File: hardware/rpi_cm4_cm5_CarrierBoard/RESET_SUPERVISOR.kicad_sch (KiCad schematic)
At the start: 34 parts, among them Q13 2N7002, Q8 2N7002, Q9 2N7002, U30 STM6710DWB6F, U31 SN74LVC1G125DBVR, U32 SN74HCS365QPWRQ1, U35 SN74HCS365QPWRQ1

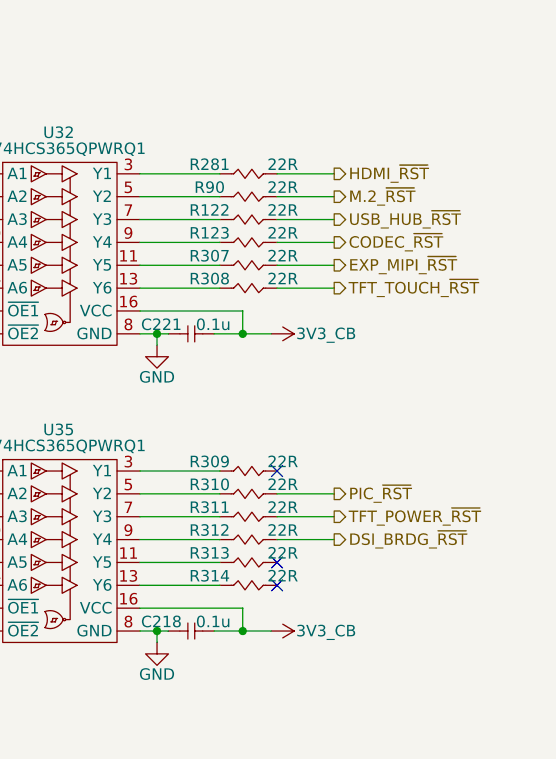
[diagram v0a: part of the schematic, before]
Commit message: Continue working on the layout. Completed most of power planes planning and pouring Completed all DiffPairs routing and length matching (preliminary)
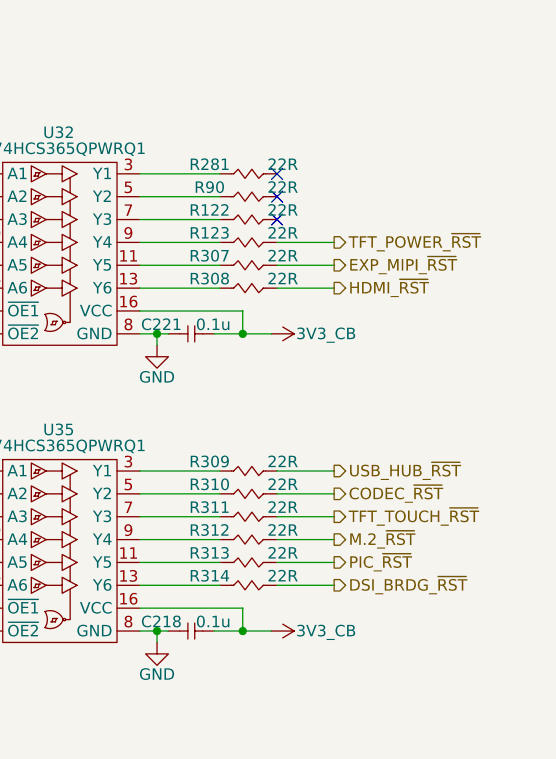
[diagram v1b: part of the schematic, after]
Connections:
- net CODEC_~{RST}: now also R310.2; no longer R123.2
- net DSI_BRDG_~{RST}: now also R314.2; no longer R312.2
- net HDMI_~{RST}: now also R308.2; no longer R281.2
- net M.2_~{RST}: now also R312.2; no longer R90.2
- net PIC_~{RST}: now also R313.2; no longer R310.2
- net TFT_POWER_~{RST}: now also R123.2; no longer R311.2
- net TFT_TOUCH_~{RST}: now also R311.2; no longer R308.2
- net USB_HUB_~{RST}: now also R309.2; no longer R122.2

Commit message: Significant update Stackup changed from 6 to 8 layers Changed design notes accordingly Re-routed all differential pairs and length match / skew match Fanout critical signals away from dense areas 95% routing completed
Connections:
- net TFT_TOUCH_~{RST}: no longer names the net of R311.2
- no-connect marks 3 -> 4
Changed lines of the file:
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@@
 	(title_block
 		(title "RPI CMx Carrier")
-		(date "2026-01-22")
+		(date "2026-02-13")
 		(rev "2.00-0A")
 		(comment 1 "Jean-Francois Bilodeau")
@@
 	)
 	(no_connect
+		(at 222.885 128.27)
+	)
+	(no_connect
 		(at 222.885 95.25)
 	)
@@
 		(pts
 			(xy 187.96 90.17) (xy 187.96 92.71)
-		)
-		(stroke
-			(width 0)
-			(type default)
-		)
-	)
-	(wire
-		(pts
-			(xy 222.885 128.27) (xy 229.235 128.27)
 		)
 		(stroke
@@
 		(effects
 			(font
-				(size 1.27 1.27)
-			)
-			(justify left)
-		)
-	)
-	(hierarchical_label "TFT_TOUCH_~{RST}"
-		(shape output)
-		(at 229.235 128.27 0)
-		(effects
-			(font

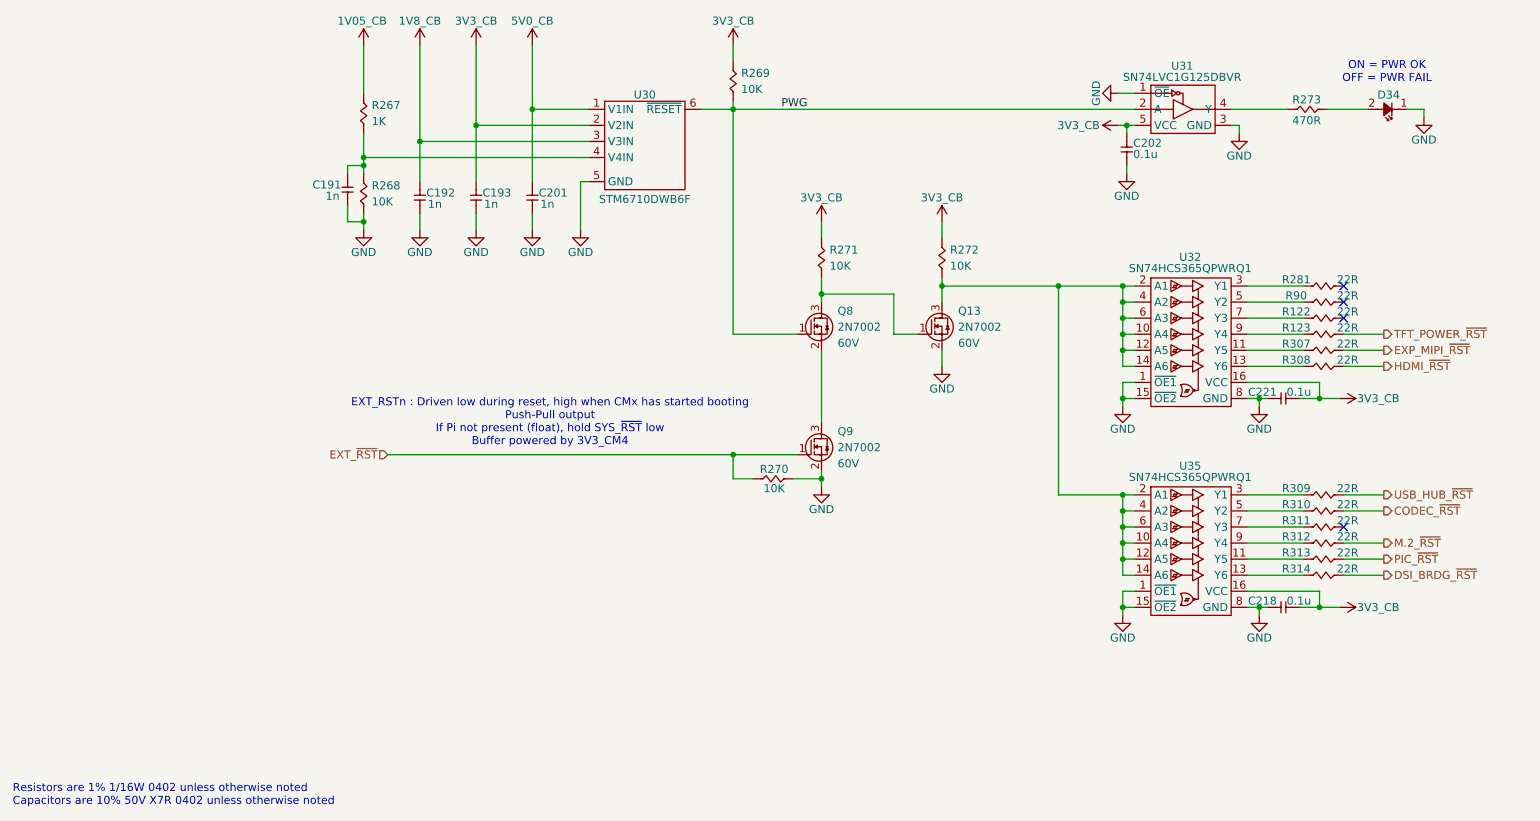
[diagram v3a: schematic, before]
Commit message: Add test points on relevant signals Re-generate SCH_PDF Re-generate BOM Re-generate all gerbers and relevant PCB output files (still in review phase)
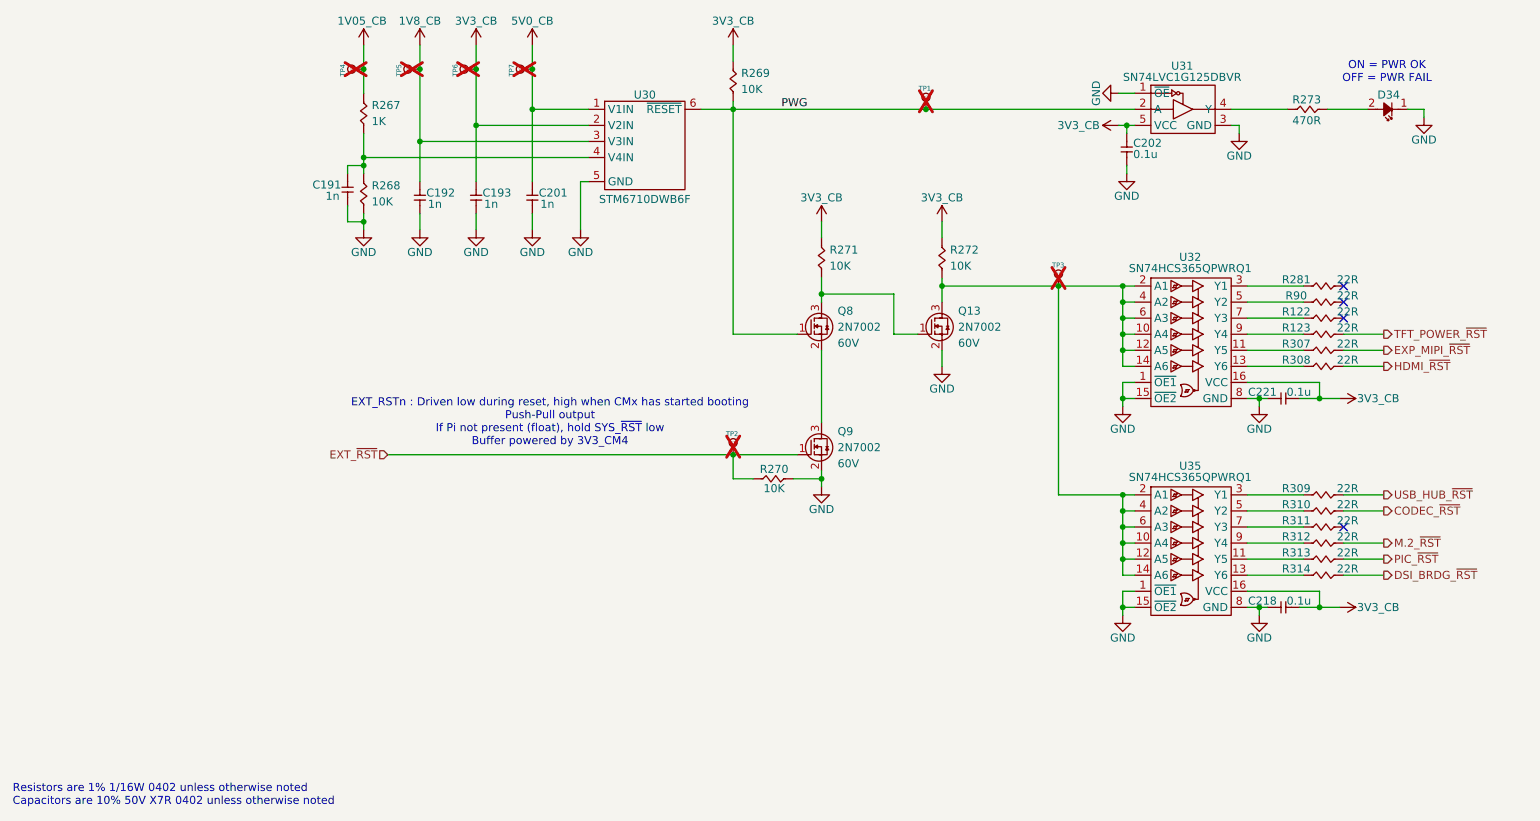
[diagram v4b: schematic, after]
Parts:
- added TP1, TP2, TP3, TP4, TP5, TP6, TP7: 28 mils, footprint:SMT_TP_28_MILS, symbol KicadCompDb:Test Point/TP_00001
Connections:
- net 1V05_CB: now also TP4.1
- net 1V8_CB: now also TP5.1
- net 3V3_CB: now also TP6.1
- net 5V0_CB: now also TP7.1
- net EXT_~{RST}: now also TP2.1
- net PWG: now also TP1.1
- net at Q13.3 (D), R272.1, U32.10 (A4)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: now also TP3.1
